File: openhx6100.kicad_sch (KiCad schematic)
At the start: 17 parts, among them J1 USB_C_Receptacle_PowerOnly_6P, Q1 MMBT3904, U1 TLC555xD

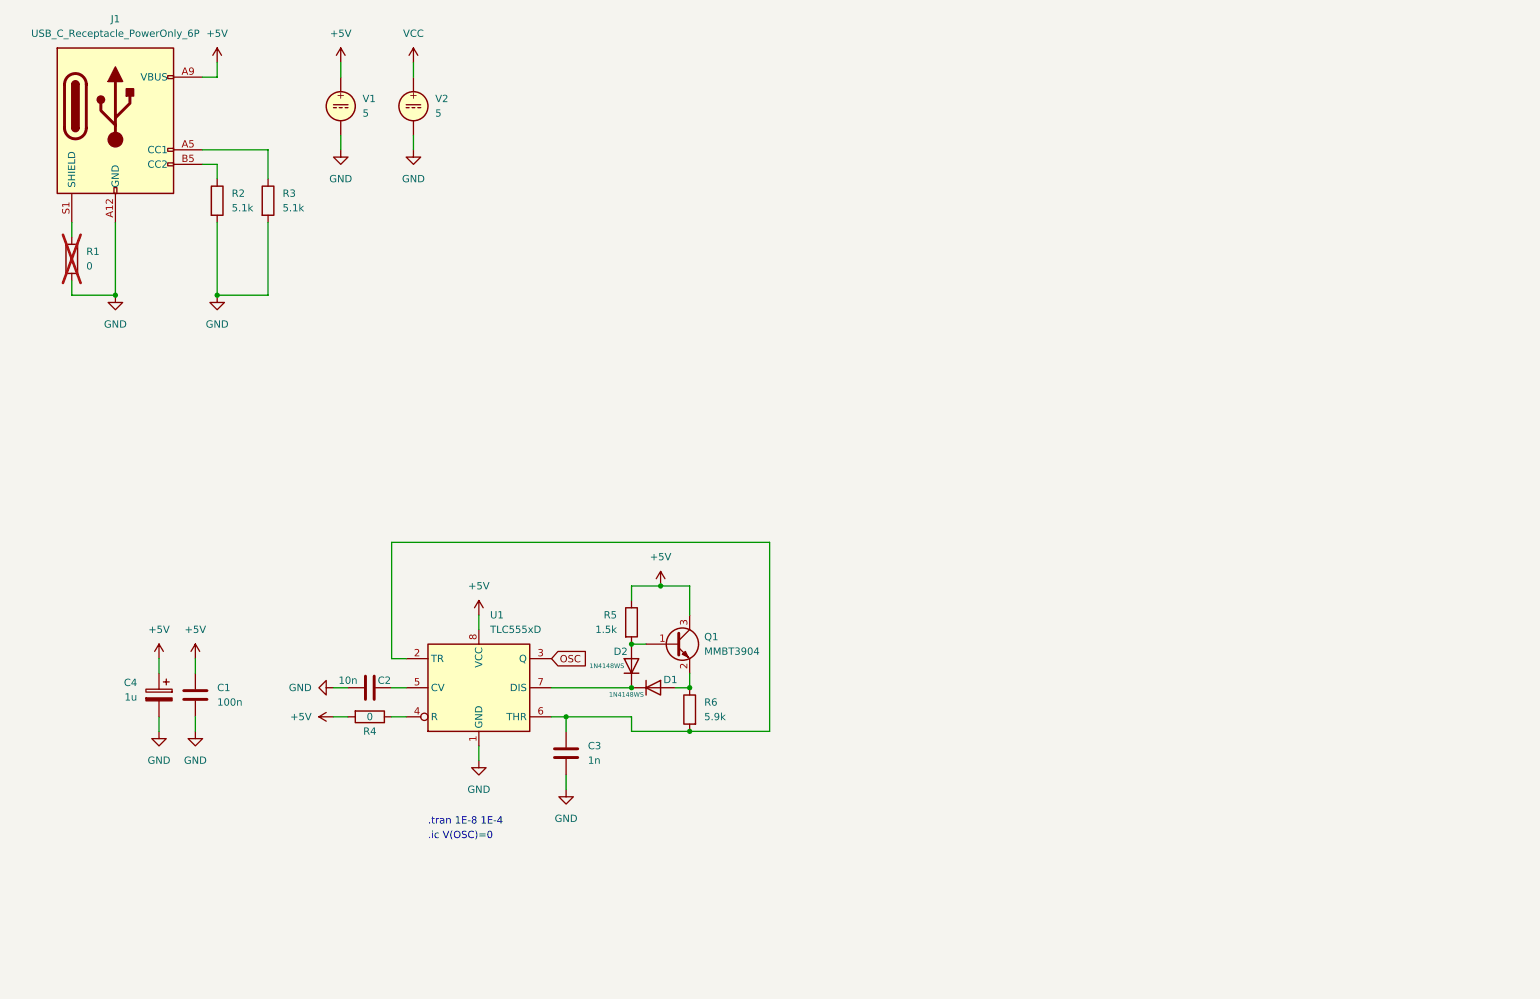
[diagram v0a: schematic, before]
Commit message: sim: switch to discrete bjt h-bridge
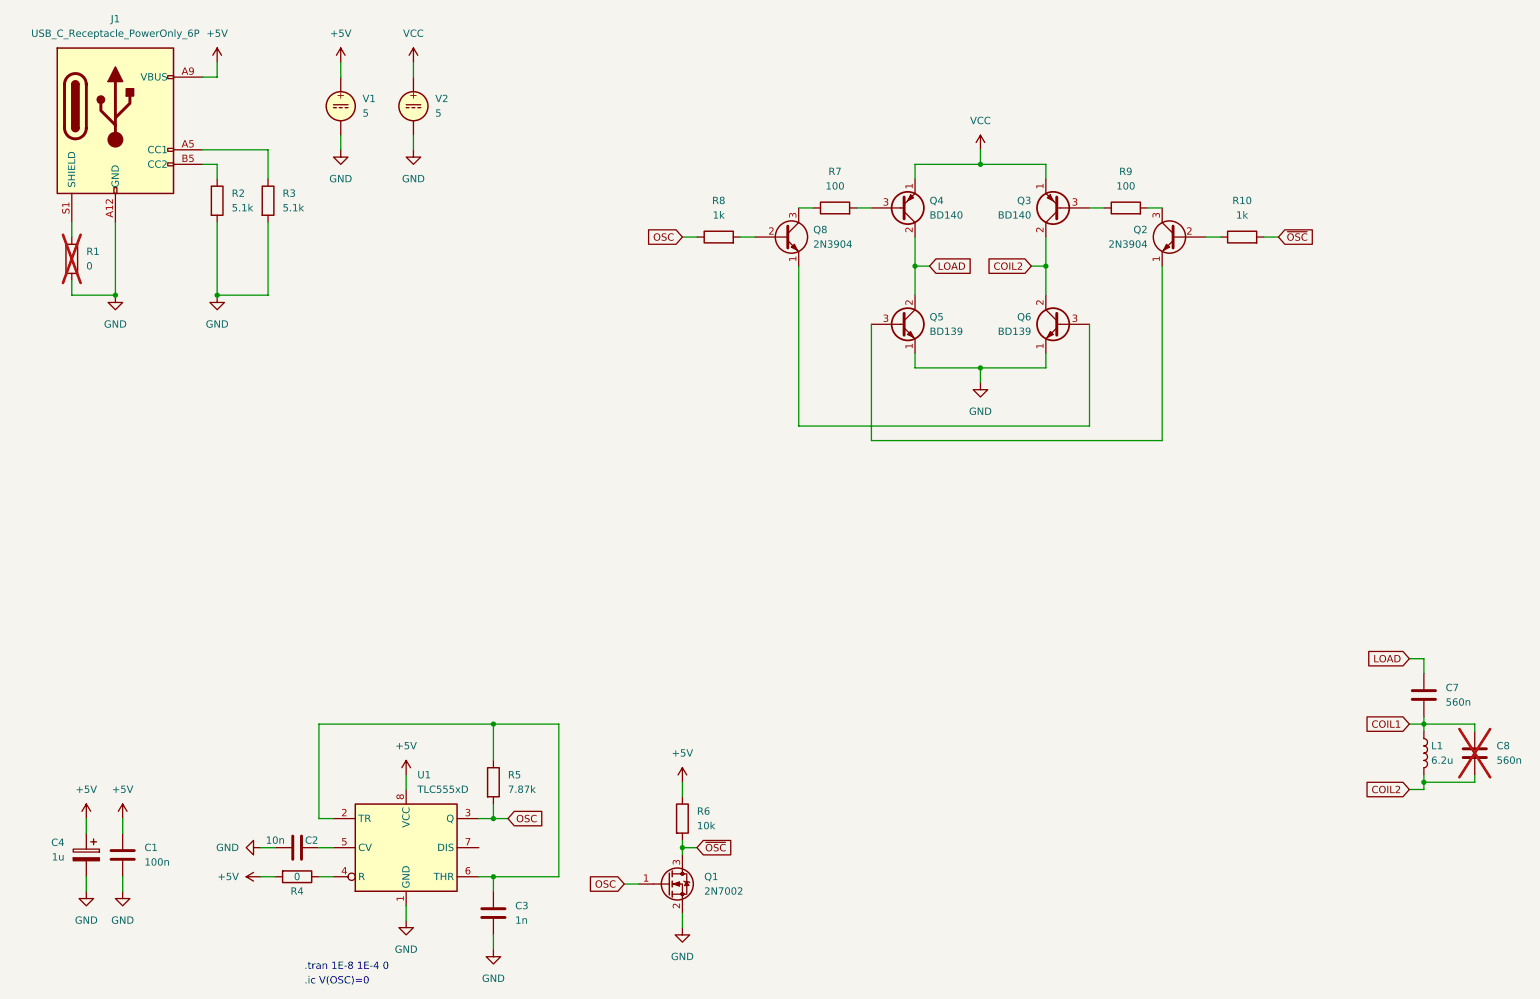
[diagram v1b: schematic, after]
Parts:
- removed D1, D2: 1N4148WS, Diode_SMD:D_SOD-323, symbol Diode:1N4148WS
- removed Q1: MMBT3904, Package_TO_SOT_SMD:SOT-23, symbol Transistor_BJT:MMBT3904
- added C7, C8: 560n, symbol Device:C
- added L1: 6.2u, symbol Device:L
- added Q1: 2N7002, Package_TO_SOT_SMD:SOT-23, symbol Transistor_FET:2N7002
- added Q2, Q8: 2N3904, Package_TO_SOT_THT:TO-92_Inline, symbol Transistor_BJT:2N3904
- added Q3, Q4: BD140, Package_TO_SOT_THT:TO-126-3_Vertical, symbol Transistor_BJT:BD140
- added Q5, Q6: BD139, Package_TO_SOT_THT:TO-126-3_Vertical, symbol Transistor_BJT:BD139
- added R10, R8: 1k, symbol Device:R
- added R7, R9: 100, symbol Device:R
- R5: value 1.5k -> 7.87k
- R6: value 5.9k -> 10k
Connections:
- net +5V: now also R6.1; no longer R5.1
- net GND: now also Q1.2 (S), Q5.1 (E), Q6.1 (E)
- net OSC: now also R5.2, Q1.1 (G), R8.1
- net VCC: now also Q3.1 (E), Q4.1 (E)
- net at C3.1, U1.2 (TR), U1.6 (THR): now also R5.1; no longer R6.2
- new net: Q3.3 (B), R9.1
- new net: Q2.3 (C), R9.2
- new net: Q6.3 (B), Q8.1 (E)
- new net: Q8.2 (B), R8.2
- new net: Q8.3 (C), R7.1
- new net: Q2.1 (E), Q5.3 (B)
- new net: Q2.2 (B), R10.1
- new net: Q4.3 (B), R7.2
- new net COIL1: C7.2, C8.1, L1.1
- new net COIL2: C8.2, L1.2, Q3.2 (C), Q6.2 (C)
- new net LOAD: C7.1, Q4.2 (C), Q5.2 (C)
- new net ~{OSC}: Q1.3 (D), R10.2, R6.2
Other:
- note added: ".tran 1E-8 1E-4 0"
- note removed: ".tran 1E-8 1E-4"
- moved on the sheet: C1, C2, C3, C4, R4, U1

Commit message: sim: switch to discrete mosfet h-bridge
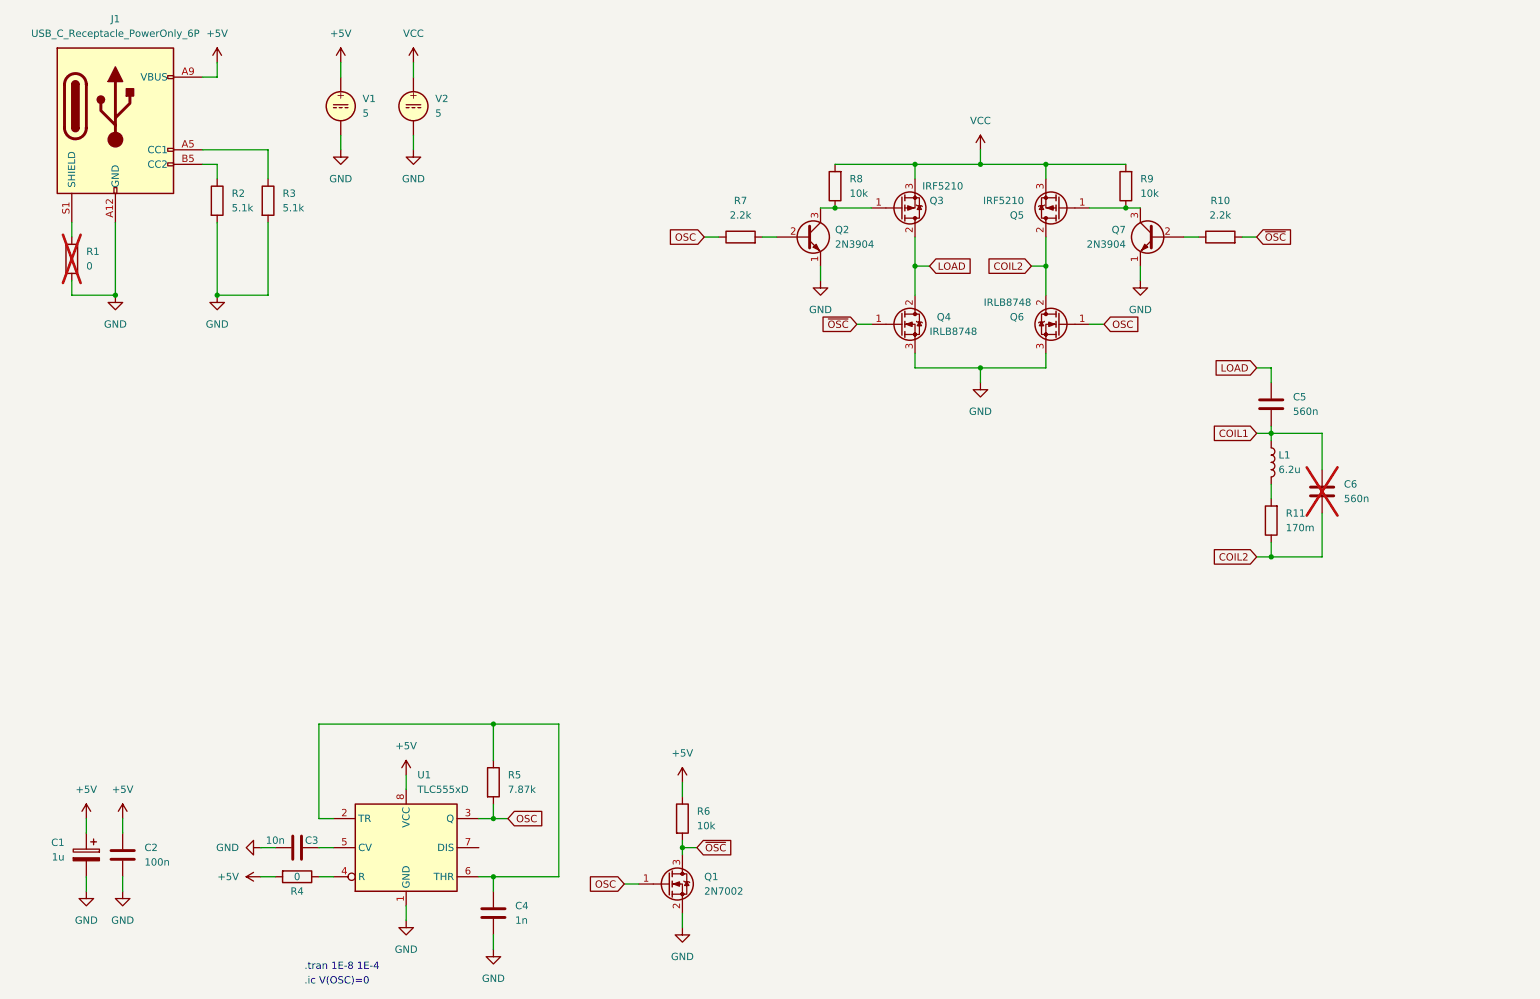
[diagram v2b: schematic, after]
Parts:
- removed Q3, Q4: BD140, Package_TO_SOT_THT:TO-126-3_Vertical, symbol Transistor_BJT:BD140
- removed Q5, Q6: BD139, Package_TO_SOT_THT:TO-126-3_Vertical, symbol Transistor_BJT:BD139
- added Q3, Q5: IRF5210, Package_TO_SOT_THT:TO-220-3_Vertical, symbol Transistor_FET:FQP27P06
- added Q4, Q6: IRLB8748, Package_TO_SOT_THT:TO-220-3_Vertical, symbol Transistor_FET:IRLB8721PBF
- added R11: 170m, symbol Device:R
- R10: value 1k -> 2.2k
- R7: renamed from R8; value 1k -> 2.2k
- R8: renamed from R7; value 100 -> 10k
- R9: value 100 -> 10k
- renumbered C4 to C1, C1 to C2, C2 to C3, C3 to C4, C7 to C5, C8 to C6, Q8 to Q2, Q2 to Q7
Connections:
- net COIL2: now also Q5.2 (D), Q6.2 (D), R11.1; no longer L1.2
- net GND: now also Q2.1 (E), Q7.1 (E), Q4.3 (S), Q6.3 (S)
- net LOAD: now also Q3.2 (D), Q4.2 (D)
- net OSC: now also Q6.1 (G)
- net VCC: now also R8.2, R9.2, Q3.3 (S), Q5.3 (S)
- net ~{OSC}: now also Q4.1 (G)
- net at R9.1: now also Q7.3 (C), Q5.1 (G)
- net at Q2.3 (C), R8.1: now also Q3.1 (G)
- new net: L1.2, R11.2
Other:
- note added: ".tran 1E-8 1E-4"
- note removed: ".tran 1E-8 1E-4 0"
- moved on the sheet: C5, C6, L1, Q2, Q7, R10, R7, R8

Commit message: layout: create pcb layout
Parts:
- removed Q1: 2N7002, Package_TO_SOT_SMD:SOT-23, symbol Transistor_FET:2N7002
- removed Q2, Q7: 2N3904, Package_TO_SOT_THT:TO-92_Inline, symbol Transistor_BJT:2N3904
- removed Q3, Q5: IRF5210, Package_TO_SOT_THT:TO-220-3_Vertical, symbol Transistor_FET:FQP27P06
- removed Q4, Q6: IRLB8748, Package_TO_SOT_THT:TO-220-3_Vertical, symbol Transistor_FET:IRLB8721PBF
- removed R10: 2.2k, symbol Device:R
- removed R11: 170m, symbol Device:R
- removed R5: 7.87k, symbol Device:R
- removed R6: 10k, symbol Device:R
- removed V1, V2: 5, symbol Simulation_SPICE:VDC
- added C6: 1u, Capacitor_SMD:CP_Elec_4x4.5, symbol Device:C_Polarized
- added C8: 100n, Capacitor_SMD:C_0805_2012Metric_Pad1.18x1.45mm_HandSolder, symbol Device:C
- added D1: GRN, LED_SMD:LED_0603_1608Metric_Pad1.05x0.95mm_HandSolder, symbol Device:LED
- added H1, H2, H3, H4: MountingHole_Pad, MountingHole:MountingHole_3.2mm_M3_DIN965_Pad, symbol Mechanical:MountingHole_Pad
- added Q1, Q3, Q7, Q8: DMG1012T, Package_TO_SOT_SMD:SOT-523, symbol Transistor_FET:DMG1012T
- added Q5, Q6: DMG2301L, Package_TO_SOT_SMD:SOT-23, symbol Transistor_FET:DMG2301L
- added R8: 150R, Resistor_SMD:R_0805_2012Metric_Pad1.20x1.40mm_HandSolder, symbol Device:R
- added RV1: 10k, Potentiometer_SMD:Potentiometer_Bourns_TC33X_Vertical, symbol Device:R_Potentiometer
- added TP1, TP2: TestPoint, TestPoint:TestPoint_Pad_4.0x4.0mm, symbol Connector:TestPoint
- added TP10, TP3, TP4, TP5, TP6, TP7, TP8, TP9: TestPoint, TestPoint:TestPoint_Keystone_5000-5004_Miniature, symbol Connector:TestPoint
- added U1: 74HC14, Package_SO:TSSOP-14_4.4x5mm_P0.65mm, symbol 74xx:74HC14
- C1: footprint (none) -> Capacitor_SMD:CP_Elec_4x4.5; DigiKey Part Number (none) -> 732-8851-1-ND
- C2: footprint (none) -> Capacitor_SMD:C_0805_2012Metric_Pad1.18x1.45mm_HandSolder; DigiKey Part Number (none) -> 399-4264-ND
- C3: footprint (none) -> Capacitor_SMD:C_0805_2012Metric_Pad1.18x1.45mm_HandSolder; DigiKey Part Number (none) -> K103K10X7RF53L2-ND
- C4: footprint (none) -> Capacitor_SMD:C_0805_2012Metric_Pad1.18x1.45mm_HandSolder; DigiKey Part Number (none) -> 445-173171-1-ND
- C5: footprint (none) -> Capacitor_SMD:C_1206_3216Metric_Pad1.33x1.80mm_HandSolder; DigiKey Part Number (none) -> 399-13965-ND
- C7: renamed from C6; footprint (none) -> Capacitor_SMD:C_1206_3216Metric_Pad1.33x1.80mm_HandSolder; DigiKey Part Number (none) -> 399-13965-ND
- J1: footprint (none) -> Gigahawk:UJC-HP-3-SMT-TR
- L1: DigiKey Part Number (none) -> 445-174580-ND; now not fitted
- R1, R2, R3, R4: footprint (none) -> Resistor_SMD:R_0805_2012Metric_Pad1.20x1.40mm_HandSolder
- R5: renamed from R8; footprint (none) -> Resistor_SMD:R_0805_2012Metric_Pad1.20x1.40mm_HandSolder; DigiKey Part Number (none) -> 13-MFR-25FRF52-10KCT-ND
- R6: renamed from R9; footprint (none) -> Resistor_SMD:R_0805_2012Metric_Pad1.20x1.40mm_HandSolder; DigiKey Part Number (none) -> 13-MFR-25FRF52-10KCT-ND
- R7: value 2.2k -> 0; footprint (none) -> Resistor_SMD:R_0805_2012Metric_Pad1.20x1.40mm_HandSolder; DigiKey Part Number (none) -> 13-MFR-25FRF52-10KCT-ND
- U2: renamed from U1; DigiKey Part Number (none) -> 296-1857-5-ND
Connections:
- net VCC is gone; now on net +5V: R5.2, R6.2
- net +5V: now also C6.1, C8.1, Q5.2 (S), Q6.2 (S), R8.1, TP6.1, U1.14 (VCC)
- net COIL1: now also TP1.1, TP9.1
- net COIL2: now also L1.2, Q6.3 (D), Q7.3 (D), TP10.1, TP2.1
- net GND: now also C6.2, C8.2, D1.1 (K), H1.1, H2.1, H3.1, H4.1, Q1.2 (S), Q3.2 (S), Q7.2 (S), Q8.2 (S), TP7.1, U1.7 (GND)
- net LOAD: now also R7.2, Q5.3 (D), Q8.3 (D), TP8.1; no longer C5.1
- net OSC: now also RV1.2, TP3.1, U1.3; no longer R7.1
- net at R6.1: now also Q3.3 (D), Q6.1 (G)
- net at R5.1: now also Q1.3 (D), Q5.1 (G)
- net SHIELD: now reaches J1.S1 (SHIELD), R1.1
- net at C4.1, U2.2 (TR), U2.6 (THR): now also RV1.1
- new net: D1.2 (A), R8.2
- new net DRIVE: Q1.1 (G), Q7.1 (G), TP4.1, U1.4, U1.5
- new net LOADR: C5.1, R7.1
- new net ~{DRIVE}: Q3.1 (G), Q8.1 (G), TP5.1, U1.6
- no-connect marks 0 -> 1
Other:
- moved on the sheet: C5, C7

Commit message: layout: finish layout
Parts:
- H1, H2, H3, H4: footprint MountingHole:MountingHole_3.2mm_M3_DIN965_Pad -> MountingHole:MountingHole_2.2mm_M2_DIN965_Pad
- Q1, Q3, Q7, Q8: footprint Package_TO_SOT_SMD:SOT-523 -> Gigahawk:SOT-523
- RV1: footprint Potentiometer_SMD:Potentiometer_Bourns_TC33X_Vertical -> Gigahawk:Potentiometer_Bourns_TC33X_Vertical
- TP10, TP3, TP4, TP5, TP6, TP7, TP8, TP9: footprint TestPoint:TestPoint_Keystone_5000-5004_Miniature -> Gigahawk:TestPoint_Keystone_5000-5004_Miniature
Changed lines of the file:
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@@
       (effects (font (size 1.27 1.27)) (justify left))
     )
-    (property "Footprint" "MountingHole:MountingHole_3.2mm_M3_DIN965_Pad" (at 176.53 107.95 0)
+    (property "Footprint" "MountingHole:MountingHole_2.2mm_M2_DIN965_Pad" (at 176.53 107.95 0)
       (effects (font (size 1.27 1.27)) hide)
     )
@@
       (effects (font (size 1.27 1.27)) (justify right))
     )
-    (property "Footprint" "Potentiometer_SMD:Potentiometer_Bourns_TC33X_Vertical" (at 105.41 154.94 0)
+    (property "Footprint" "Gigahawk:Potentiometer_Bourns_TC33X_Vertical" (at 105.41 154.94 0)
       (effects (font (size 1.27 1.27)) hide)
     )
@@
       (effects (font (size 1.27 1.27)) (justify left))
     )
-    (property "Footprint" "MountingHole:MountingHole_3.2mm_M3_DIN965_Pad" (at 176.53 102.87 0)
+    (property "Footprint" "MountingHole:MountingHole_2.2mm_M2_DIN965_Pad" (at 176.53 102.87 0)
       (effects (font (size 1.27 1.27)) hide)
     )
@@
       (effects (font (size 1.27 1.27)))
     )
-    (property "Footprint" "TestPoint:TestPoint_Keystone_5000-5004_Miniature" (at 147.32 142.24 0)
+    (property "Footprint" "Gigahawk:TestPoint_Keystone_5000-5004_Miniature" (at 147.32 142.24 0)
       (effects (font (size 1.27 1.27)) hide)
     )
@@
       (effects (font (size 1.27 1.27)))
     )
-    (property "Footprint" "TestPoint:TestPoint_Keystone_5000-5004_Miniature" (at 147.32 149.86 0)
+    (property "Footprint" "Gigahawk:TestPoint_Keystone_5000-5004_Miniature" (at 147.32 149.86 0)
       (effects (font (size 1.27 1.27)) hide)
     )
@@
       (effects (font (size 1.27 1.27)) (justify left))
     )
-    (property "Footprint" "Package_TO_SOT_SMD:SOT-523" (at 195.58 76.835 0)
+    (property "Footprint" "Gigahawk:SOT-523" (at 195.58 76.835 0)
       (effects (font (size 1.27 1.27)) (justify left) hide)
     )
@@
       (effects (font (size 1.27 1.27)))
     )
-    (property "Footprint" "TestPoint:TestPoint_Keystone_5000-5004_Miniature" (at 147.32 104.14 0)
+    (property "Footprint" "Gigahawk:TestPoint_Keystone_5000-5004_Miniature" (at 147.32 104.14 0)
       (effects (font (size 1.27 1.27)) hide)
     )
@@
       (effects (font (size 1.27 1.27)))
     )
-    (property "Footprint" "TestPoint:TestPoint_Keystone_5000-5004_Miniature" (at 147.32 119.38 0)
+    (property "Footprint" "Gigahawk:TestPoint_Keystone_5000-5004_Miniature" (at 147.32 119.38 0)
       (effects (font (size 1.27 1.27)) hide)
     )
@@
       (effects (font (size 1.27 1.27)))
     )
-    (property "Footprint" "TestPoint:TestPoint_Keystone_5000-5004_Miniature" (at 147.32 111.76 0)
+    (property "Footprint" "Gigahawk:TestPoint_Keystone_5000-5004_Miniature" (at 147.32 111.76 0)
       (effects (font (size 1.27 1.27)) hide)
     )
@@
       (effects (font (size 1.27 1.27)))
     )
-    (property "Footprint" "TestPoint:TestPoint_Keystone_5000-5004_Miniature" (at 147.32 96.52 0)
+    (property "Footprint" "Gigahawk:TestPoint_Keystone_5000-5004_Miniature" (at 147.32 96.52 0)
       (effects (font (size 1.27 1.27)) hide)
     )
@@
       (effects (font (size 1.27 1.27)))
     )
-    (property "Footprint" "TestPoint:TestPoint_Keystone_5000-5004_Miniature" (at 147.32 134.62 0)
+    (property "Footprint" "Gigahawk:TestPoint_Keystone_5000-5004_Miniature" (at 147.32 134.62 0)
       (effects (font (size 1.27 1.27)) hide)
     )
@@
       (effects (font (size 1.27 1.27)) (justify left))
     )
-    (property "Footprint" "MountingHole:MountingHole_3.2mm_M3_DIN965_Pad" (at 176.53 113.03 0)
+    (property "Footprint" "MountingHole:MountingHole_2.2mm_M2_DIN965_Pad" (at 176.53 113.03 0)
       (effects (font (size 1.27 1.27)) hide)
     )
@@
       (effects (font (size 1.27 1.27)) (justify left))
     )
-    (property "Footprint" "Package_TO_SOT_SMD:SOT-523" (at 177.8 76.835 0)
+    (property "Footprint" "Gigahawk:SOT-523" (at 177.8 76.835 0)
       (effects (font (size 1.27 1.27)) (justify left) hide)
     )
@@
       (effects (font (size 1.27 1.27)))
     )
-    (property "Footprint" "TestPoint:TestPoint_Keystone_5000-5004_Miniature" (at 147.32 127 0)
+    (property "Footprint" "Gigahawk:TestPoint_Keystone_5000-5004_Miniature" (at 147.32 127 0)
       (effects (font (size 1.27 1.27)) hide)
     )
@@
       (effects (font (size 1.27 1.27)) (justify left))
     )
-    (property "Footprint" "Package_TO_SOT_SMD:SOT-523" (at 212.09 61.595 0)
+    (property "Footprint" "Gigahawk:SOT-523" (at 212.09 61.595 0)
       (effects (font (size 1.27 1.27)) (justify left) hide)
     )
@@
       (effects (font (size 1.27 1.27)) (justify left))
     )
-    (property "Footprint" "Package_TO_SOT_SMD:SOT-523" (at 161.29 61.595 0)
+    (property "Footprint" "Gigahawk:SOT-523" (at 161.29 61.595 0)
       (effects (font (size 1.27 1.27)) (justify left) hide)
     )
@@
       (effects (font (size 1.27 1.27)) (justify left))
     )
-    (property "Footprint" "MountingHole:MountingHole_3.2mm_M3_DIN965_Pad" (at 176.53 118.11 0)
-      (effects (font (size 1.27 1.27)) hide)
-    )
+    (property "Footprint" "MountingHole:MountingHole_2.2mm_M2_DIN965_Pad" (at 176.53 118.11 0)
+      (effects (font (size 1.27 1.27)) hide)
+    )
